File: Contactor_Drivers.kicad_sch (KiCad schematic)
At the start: 37 parts, among them Con1 LED, Con2 LED, Con3 LED, Con4 LED, J3 Conn_01x05, J4 Conn_01x04, J5 Conn_01x04, J6 Conn_01x04, J7 Conn_01x04, Q4 IRLML0030, Q5 IRLML0030, Q6 IRLML0030, Q7 IRLML0030

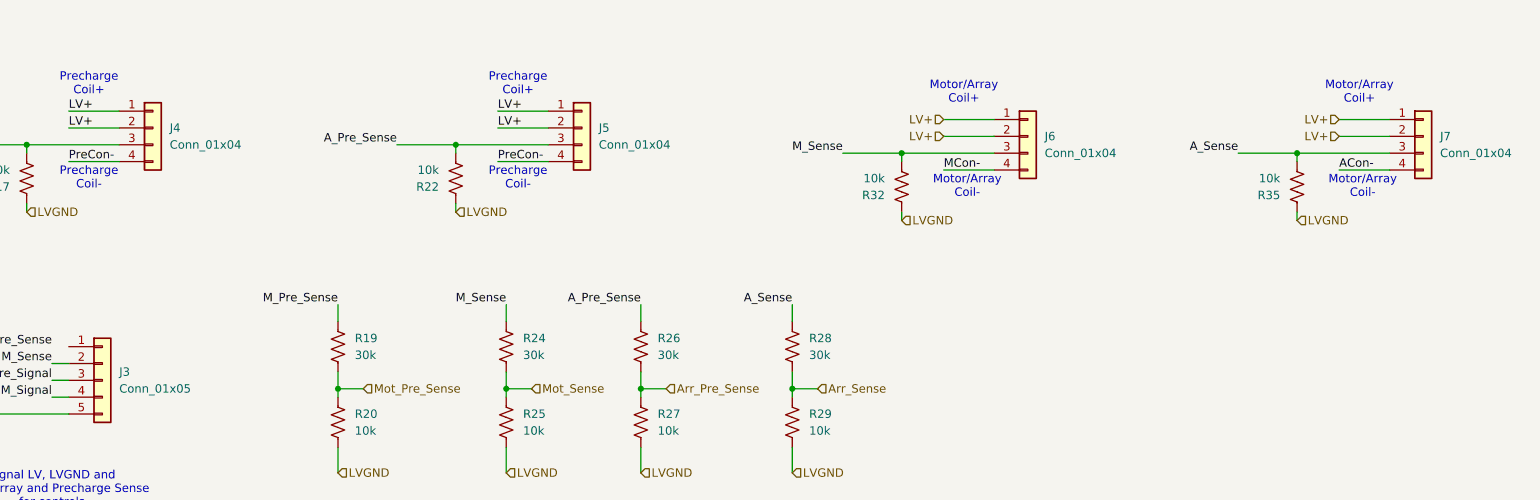
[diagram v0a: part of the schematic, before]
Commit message: parts sheet and cost estimate
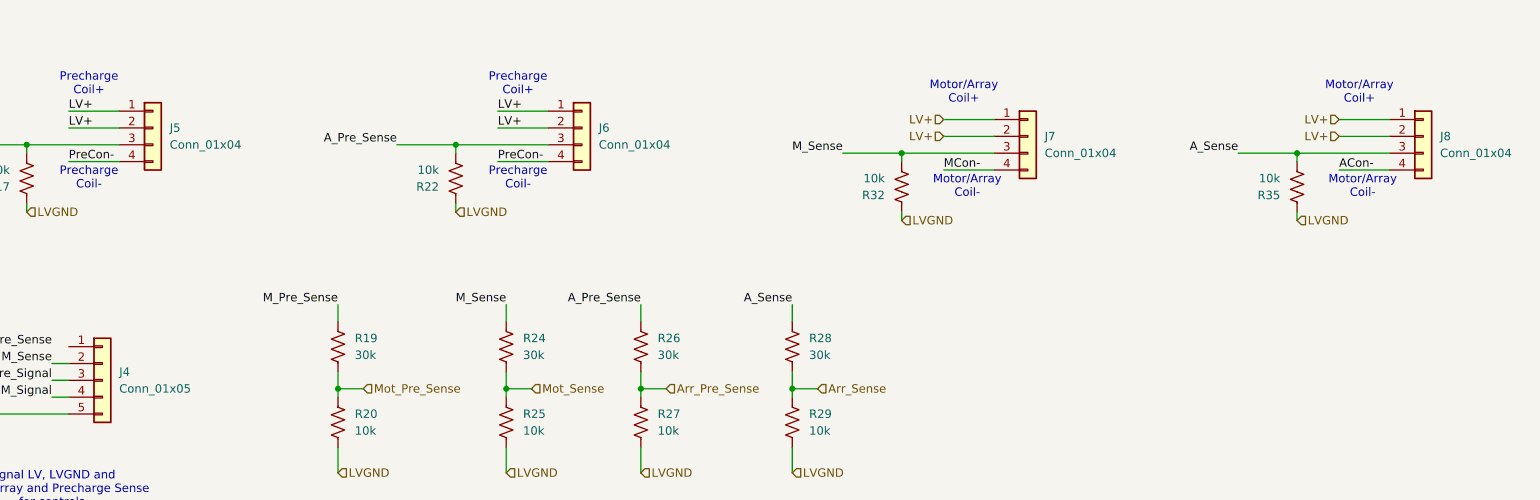
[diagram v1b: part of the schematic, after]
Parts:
- J4: renamed from J3; footprint (none) -> utsvt-conn:Molex_MicroFit_01x06_Horizontal
- R19, R20, R24, R25, R26, R27, R28, R29: footprint (none) -> Resistor_SMD:R_0805_2012Metric
- renumbered J4 to J5, J5 to J6, J6 to J7, J7 to J8
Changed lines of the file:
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@@
 			)
 		)
-		(property "Footprint" ""
+		(property "Footprint" "Resistor_SMD:R_0805_2012Metric"
 			(at 102.616 141.224 90)
 			(effects
@@
 			)
 		)
-		(property "Footprint" ""
+		(property "Footprint" "Resistor_SMD:R_0805_2012Metric"
 			(at 102.616 152.654 90)
 			(effects
@@
 			)
 		)
-		(property "Footprint" ""
+		(property "Footprint" "Resistor_SMD:R_0805_2012Metric"
 			(at 171.196 141.224 90)
 			(effects
@@
 			)
 		)
-		(property "Footprint" ""
+		(property "Footprint" "Resistor_SMD:R_0805_2012Metric"
 			(at 128.016 152.654 90)
 			(effects
@@
 			)
 		)
-		(property "Footprint" ""
+		(property "Footprint" "Resistor_SMD:R_0805_2012Metric"
 			(at 128.016 141.224 90)
 			(effects
@@
 			)
 		)
-		(property "Footprint" ""
+		(property "Footprint" "Resistor_SMD:R_0805_2012Metric"
 			(at 171.196 152.654 90)
 			(effects
@@
 		(dnp no)
 		(fields_autoplaced yes)
-		(property "Reference" "J7"
+		(property "Reference" "J8"
 			(at 267.97 109.2199 0)
 			(effects
@@
 			(project "ActivePrecharge"
 				(path "/b9847a31-2b3b-47ca-9561-fab506416f6d/c0036b4f-8078-47a1-85ab-72dbdcf28d35"
-					(reference "J7")
+					(reference "J8")
 					(unit 1)
 				)
@@
 			)
 		)
-		(property "Footprint" ""
+		(property "Footprint" "Resistor_SMD:R_0805_2012Metric"
 			(at 148.336 141.224 90)
 			(effects
@@
 			)
 		)
-		(property "Footprint" ""
+		(property "Footprint" "Resistor_SMD:R_0805_2012Metric"
 			(at 148.336 152.654 90)
 			(effects
@@
 		(dnp no)
 		(fields_autoplaced yes)
-		(property "Reference" "J4"
+		(property "Reference" "J5"
 			(at 76.2 107.9499 0)
 			(effects
@@
 			(project "ActivePrecharge"
 				(path "/b9847a31-2b3b-47ca-9561-fab506416f6d/c0036b4f-8078-47a1-85ab-72dbdcf28d35"
-					(reference "J4")
+					(reference "J5")
 					(unit 1)
 				)
@@
 		(dnp no)
 		(fields_autoplaced yes)
-		(property "Reference" "J3"
+		(property "Reference" "J4"
 			(at 68.58 144.7799 0)
 			(effects
@@
 			)
 		)
-		(property "Footprint" ""
+		(property "Footprint" "utsvt-conn:Molex_MicroFit_01x06_Horizontal"
 			(at 66.04 146.05 0)
 			(effects
@@
 			(project ""
 				(path "/b9847a31-2b3b-47ca-9561-fab506416f6d/c0036b4f-8078-47a1-85ab-72dbdcf28d35"
-					(reference "J3")
+					(reference "J4")
 					(unit 1)
 				)
@@
 		(dnp no)
 		(fields_autoplaced yes)
-		(property "Reference" "J6"
+		(property "Reference" "J7"
 			(at 208.28 109.2199 0)
 			(effects
@@
 			(project "ActivePrecharge"
 				(path "/b9847a31-2b3b-47ca-9561-fab506416f6d/c0036b4f-8078-47a1-85ab-72dbdcf28d35"
-					(reference "J6")
+					(reference "J7")
 					(unit 1)
 				)
@@
 		(dnp no)
 		(fields_autoplaced yes)
-		(property "Reference" "J5"
+		(property "Reference" "J6"
 			(at 140.97 107.9499 0)
 			(effects
@@
 			(project "ActivePrecharge"
 				(path "/b9847a31-2b3b-47ca-9561-fab506416f6d/c0036b4f-8078-47a1-85ab-72dbdcf28d35"
-					(reference "J5")
-					(unit 1)
-				)
+					(reference "J6")
+					(unit 1)
+				)
